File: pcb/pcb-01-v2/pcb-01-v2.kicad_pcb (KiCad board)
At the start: 2 copper layers, 0 parts

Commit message: Complete PCB-01 V2 KiCad scaffold
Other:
- copper layers 2 -> 4
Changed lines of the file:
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@@
 	)
 	(paper "A4")
+	(title_block
+		(title "PCB-01 V2 Controller")
+		(rev "V2")
+		(company "Stillair")
+		(comment 1 "Fresh 4-layer controller redesign")
+	)
 	(layers
 		(0 "F.Cu" signal)
+		(4 "In1.Cu" power)
+		(6 "In2.Cu" power)
 		(2 "B.Cu" signal)
 		(9 "F.Adhes" user "F.Adhesive")
@@
 	)
 	(setup
+		(stackup
+			(layer "F.SilkS"
+				(type "Top Silk Screen")
+			)
+			(layer "F.Paste"
+				(type "Top Solder Paste")
+			)
+			(layer "F.Mask"
+				(type "Top Solder Mask")
+				(thickness 0.01)
+			)
+			(layer "F.Cu"
+				(type "copper")
+				(thickness 0.07)
+			)
+			(layer "dielectric 1"
+				(type "prepreg")
+				(thickness 0.1)
+				(material "FR4")
+				(epsilon_r 4.5)
+				(loss_tangent 0.02)
+			)
+			(layer "In1.Cu"
+				(type "copper")
+				(thickness 0.035)
+			)
+			(layer "dielectric 2"
+				(type "core")
+				(thickness 1.17)
+				(material "FR4")
+				(epsilon_r 4.5)
+				(loss_tangent 0.02)
+			)
+			(layer "In2.Cu"
+				(type "copper")
+				(thickness 0.035)
+			)
+			(layer "dielectric 3"
+				(type "prepreg")
+				(thickness 0.1)
+				(material "FR4")
+				(epsilon_r 4.5)
+				(loss_tangent 0.02)
+			)
+			(layer "B.Cu"
+				(type "copper")
+				(thickness 0.07)
+			)
+			(layer "B.Mask"
+				(type "Bottom Solder Mask")
+				(thickness 0.01)
+			)
+			(layer "B.Paste"
+				(type "Bottom Solder Paste")
+			)
+			(layer "B.SilkS"
+				(type "Bottom Silk Screen")
+			)
+			(copper_finish "None")
+			(dielectric_constraints no)
+		)
 		(pad_to_mask_clearance 0.05)
 		(allow_soldermask_bridges_in_footprints no)
@@
 		(capping no)
 		(filling no)
+		(zone_defaults)
 		(pcbplotparams
 			(layerselection 0x00000000_00000000_55555555_5755f5ff)

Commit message: Build PCB-01 V2 ready-to-route project
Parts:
- added C1: 470uF 50V, Capacitor_THT:CP_Radial_D10.0mm_P5.00mm, F.Cu at (58.5, 64.5)
- added C10: 22uF 25V X7R 10%, Capacitor_SMD:C_1210_3225Metric, F.Cu at (91.0, 63.0)
- added C11: 1uF 50V X5R 10%, Capacitor_SMD:C_0603_1608Metric, F.Cu at (84.0, 57.5)
- added C12: 1uF 50V X5R 10%, Capacitor_SMD:C_0603_1608Metric, F.Cu at (80.3, 92.8)
- added C13: 47nF 100V X7R 10%, Capacitor_SMD:C_0805_2012Metric, F.Cu at (78.0, 88.0)
- added C14: 1uF 50V X5R 10%, Capacitor_SMD:C_0603_1608Metric, F.Cu at (88.4, 93.8)
- added C15: 1uF 50V X5R 10%, Capacitor_SMD:C_0603_1608Metric, F.Cu at (83.6, 88.3)
- added C16: 22uF 25V X7R 10%, Capacitor_SMD:C_1210_3225Metric, F.Cu at (69.8, 94.0)
- added C17: 22uF 25V X7R 10%, Capacitor_SMD:C_1210_3225Metric, F.Cu at (128.5, 61.5)
- added C18: 100nF 16V X7R 10%, Capacitor_SMD:C_0402_1005Metric, F.Cu at (123.0, 63.8)
- added C19: 1uF 25V X5R 10%, Capacitor_SMD:C_0402_1005Metric, F.Cu at (124.5, 63.8)
- added C2: 470uF 50V, Capacitor_THT:CP_Radial_D10.0mm_P5.00mm, F.Cu at (71.5, 64.5)
- added C20: 100nF 16V X7R 10% U12 bypass, Capacitor_SMD:C_0402_1005Metric, F.Cu at (120.5, 61.5)
- added C22: 100nF 16V X7R 10%, Capacitor_SMD:C_0402_1005Metric, F.Cu at (97.5, 99.0)
- added C23: 10uF 25V X5R 10%, Capacitor_SMD:C_0805_2012Metric, F.Cu at (104.0, 85.0)
- added C24: 100nF 16V X7R 10%, Capacitor_SMD:C_0402_1005Metric, F.Cu at (103.5, 100.0)
- added C25: 100nF 16V X7R 10%, Capacitor_SMD:C_0402_1005Metric, F.Cu at (105.3, 95.7)
- added C26: 10uF 63V X7R 10%, Capacitor_SMD:C_1210_3225Metric, F.Cu at (116.8, 104.0)
- added C27: 100nF 100V X7R 10%, Capacitor_SMD:C_0805_2012Metric, F.Cu at (105.7, 103.7)
- added C28: 10uF 25V X7R 10%, Capacitor_SMD:C_1210_3225Metric, F.Cu at (106.5, 108.6)
- added C29: 100nF 50V X7R 10%, Capacitor_SMD:C_0603_1608Metric, F.Cu at (125.8, 100.5)
- added C3: 10uF 50V X7R 10%, Capacitor_SMD:C_1210_3225Metric, F.Cu at (79.0, 100.5)
- added C30: 10nF 50V C0G 5%, Capacitor_SMD:C_0603_1608Metric, F.Cu at (111.0, 99.0)
- added C31: 10nF 50V X7R 10%, Capacitor_SMD:C_0402_1005Metric, F.Cu at (113.5, 100.8)
- added C33: 100nF 50V X7R 10%, Capacitor_SMD:C_0603_1608Metric, F.Cu at (126.3, 96.0)
- added C34: 100nF 50V C0G 1%, Capacitor_SMD:C_1206_3216Metric, F.Cu at (115.0, 94.0)
- added C35: 2.2uF 50V X5R 10%, Capacitor_SMD:C_0805_2012Metric, F.Cu at (116.0, 99.0)
- added C4: 10uF 50V X7R 10%, Capacitor_SMD:C_1210_3225Metric, F.Cu at (78.0, 78.5)
- added C41: 100nF 16V X7R 10%, Capacitor_SMD:C_0402_1005Metric, F.Cu at (133.3, 100.2)
- added C42: 100nF 16V X7R 10%, Capacitor_SMD:C_0402_1005Metric, F.Cu at (99.2, 81.5)
- added C43: 100nF 16V X7R 10%, Capacitor_SMD:C_0402_1005Metric, F.Cu at (106.2, 87.2)
- added C5: 100nF 50V X7R 10%, Capacitor_SMD:C_0603_1608Metric, F.Cu at (80.3, 96.0)
- added C7: 2.2uF 100V X7R 10%, Capacitor_SMD:C_1210_3225Metric, F.Cu at (76.5, 57.5)
- added C8: 100nF 100V X7R 10%, Capacitor_SMD:C_0805_2012Metric, F.Cu at (81.0, 61.0)
- added C9: 22uF 25V X7R 10%, Capacitor_SMD:C_1210_3225Metric, F.Cu at (91.5, 59.0)
- added D1: MMSZ5242B-7-F, Diode_SMD:D_SOD-123, F.Cu at (56.5, 84.5)
- added D2: SMCJ24A, Diode_SMD:D_SMC, F.Cu at (66.5, 87.0)
- added D3: BAT54W-G3-08, Diode_SMD:D_SOD-123, F.Cu at (89.5, 75.0)
- added D4: BAT54W-G3-08, Diode_SMD:D_SOD-123, F.Cu at (94.5, 75.0)
- added D5: BAT54W-G3-08, Diode_SMD:D_SOD-123, F.Cu at (99.5, 75.0)
- added D6: BAT54W-G3-08, Diode_SMD:D_SOD-123, F.Cu at (94.0, 78.5)
- added D7: BAT54W-G3-08, Diode_SMD:D_SOD-123, F.Cu at (90.0, 85.0)
- added D8: BAT54W-G3-08, Diode_SMD:D_SOD-123, F.Cu at (106.0, 82.0)
- added D9: BAT54SLT1G, Package_TO_SOT_SMD:SOT-23, F.Cu at (110.0, 96.0)
- added FID1: FIDUCIAL, Fiducial_1mm_Mask2mm, F.Cu at (125.0, 53.9)
- added FID2: FIDUCIAL, Fiducial_1mm_Mask2mm, F.Cu at (134.2, 62.0)
- added FID3: FIDUCIAL, Fiducial_1mm_Mask2mm, F.Cu at (63.0, 103.0)
- added H1: M3 NPTH, MountingHole_M3_3.2mm, F.Cu at (55.0, 55.0)
- added H2: M3 NPTH, MountingHole_M3_3.2mm, F.Cu at (133.0, 55.0)
- added H3: M3 NPTH, MountingHole_M3_3.2mm, F.Cu at (55.0, 109.0)
- added H4: M3 NPTH, MountingHole_M3_3.2mm, F.Cu at (133.0, 109.0)
- added J1: 43045-0200 POWER, Connector_Molex:Molex_Micro-Fit_3.0_43045-0200_2x01_P3.00mm_Horizontal, F.Cu at (56.5, 77.0)
- added J2: 43650-0300, Connector_Molex:Molex_Micro-Fit_3.0_43650-0300_1x03_P3.00mm_Horizontal, F.Cu at (88.5, 104.5)
- added J3: B3B-PH-K-S(LF)(SN), Connector_JST:JST_PH_B3B-PH-K_1x03_P2.00mm_Vertical, F.Cu at (118.0, 110.5)
- added J5: B5B-PH-K-S(LF)(SN), Connector_JST:JST_PH_B5B-PH-K_1x05_P2.00mm_Vertical, F.Cu at (91.0, 52.5)
- added L1: SWPA6045S470MT, Inductor_SMD:L_Sunlord_SWPA6045S, F.Cu at (76.0, 94.0)
- added NT1: PGND-AGND tie, NetTie:NetTie-2_SMD_Pad2.0mm, F.Cu at (84.0, 85.5)
- added Q1: DMP6023LE-13, Package_TO_SOT_SMD:SOT-223-3_TabPin2, F.Cu at (66.5, 77.0)
- added Q2: 2N7002K-7, Package_TO_SOT_SMD:SOT-23, F.Cu at (94.0, 91.0)
- added Q3: 2N7002K-7, Package_TO_SOT_SMD:SOT-23, F.Cu at (115.0, 88.5)
- added Q4: BC847BDW1T1G, Package_TO_SOT_SMD:SOT-363_SC-70-6, F.Cu at (109.5, 62.0)
- added R1: 10k, Resistor_SMD:R_0402_1005Metric, F.Cu at (60.5, 83.5)
- added R10: 100k 1%, Resistor_SMD:R_0402_1005Metric, F.Cu at (93.0, 88.5)
- added R11: 10k 1%, Resistor_SMD:R_0402_1005Metric, F.Cu at (103.0, 74.5)
- added R12: 10k 1%, Resistor_SMD:R_0402_1005Metric, F.Cu at (105.0, 74.5)
- added R13: 10k 1%, Resistor_SMD:R_0402_1005Metric, F.Cu at (103.0, 76.5)
- added R14: 100ohm 1%, Resistor_SMD:R_0402_1005Metric, F.Cu at (88.5, 81.0)
- added R15: 100ohm 1%, Resistor_SMD:R_0402_1005Metric, F.Cu at (90.7, 81.0)
- added R16: 0ohm I2C isolation link, Resistor_SMD:R_0402_1005Metric, F.Cu at (88.5, 83.0)
- added R17: 0ohm I2C isolation link, Resistor_SMD:R_0402_1005Metric, F.Cu at (90.7, 83.0)
- added R18: 10k 1%, Resistor_SMD:R_0402_1005Metric, F.Cu at (105.0, 76.5)
- added R19: 4.7k 1%, Resistor_SMD:R_0402_1005Metric, F.Cu at (113.0, 63.0)
- added R2: 100k, Resistor_SMD:R_0402_1005Metric, F.Cu at (60.5, 85.5)
- added R20: 4.7k 1%, Resistor_SMD:R_0402_1005Metric, F.Cu at (116.0, 63.0)
- added R24: 100ohm 1%, Resistor_SMD:R_0402_1005Metric, F.Cu at (93.0, 86.0)
- added R25: 100k 1%, Resistor_SMD:R_0402_1005Metric, F.Cu at (96.0, 86.0)
- added R26: 1k 1%, Resistor_SMD:R_0402_1005Metric, F.Cu at (91.0, 90.0)
- added R27: 100k 1%, Resistor_SMD:R_0402_1005Metric, F.Cu at (91.0, 92.0)
- added R28: 4.7k 1%, Resistor_SMD:R_0402_1005Metric, F.Cu at (89.0, 97.5)
- added R29: 10k 1%, Resistor_SMD:R_0402_1005Metric, F.Cu at (91.0, 96.0)
- added R3: 10k 1%, Resistor_SMD:R_0402_1005Metric, F.Cu at (91.0, 66.5)
- added R30: 10k 1%, Resistor_SMD:R_0402_1005Metric, F.Cu at (93.0, 96.0)
- added R31: 100k 1%, Resistor_SMD:R_0402_1005Metric, F.Cu at (95.0, 96.0)
- added R32: 10k 1%, Resistor_SMD:R_0402_1005Metric, F.Cu at (97.0, 93.0)
- added R33: 10k 1%, Resistor_SMD:R_0402_1005Metric, F.Cu at (99.0, 93.0)
- added R34: 10k 1%, Resistor_SMD:R_0402_1005Metric, F.Cu at (97.0, 95.0)
- added R35: 10k 1%, Resistor_SMD:R_0402_1005Metric, F.Cu at (99.0, 95.0)
- added R36: 100ohm 1%, Resistor_SMD:R_0402_1005Metric, F.Cu at (97.0, 97.0)
- added R37: 10k 1%, Resistor_SMD:R_0402_1005Metric, F.Cu at (99.0, 97.0)
- added R38: 100ohm 1%, Resistor_SMD:R_0402_1005Metric, F.Cu at (104.0, 91.0)
- added R39: 47ohm 1W 1%, Resistor_SMD:R_2512_6332Metric, F.Cu at (84.5, 69.5)
- added R4: 4.7k 1%, Resistor_SMD:R_0402_1005Metric, F.Cu at (85.0, 77.0)
- added R40: 910k 0.1%, Resistor_SMD:R_0402_1005Metric, F.Cu at (108.0, 87.0)
- added R41: 100k 0.1%, Resistor_SMD:R_0402_1005Metric, F.Cu at (110.0, 87.0)
- added R42: 10k 1%, Resistor_SMD:R_0402_1005Metric, F.Cu at (108.0, 89.0)
- added R43: 10k 1%, Resistor_SMD:R_0402_1005Metric, F.Cu at (110.0, 89.0)
- added R44: 10k 1%, Resistor_SMD:R_0402_1005Metric, F.Cu at (108.0, 91.0)
- added R45: 100ohm 1%, Resistor_SMD:R_0402_1005Metric, F.Cu at (110.0, 91.0)
- added R46: 10k 1%, Resistor_SMD:R_0402_1005Metric, F.Cu at (108.0, 93.0)
- added R47: 10k 1%, Resistor_SMD:R_0402_1005Metric, F.Cu at (110.0, 93.0)
- added R48: 562k 1%, Resistor_SMD:R_0402_1005Metric, F.Cu at (121.0, 103.0)
- added R49: 10k 1%, Resistor_SMD:R_0402_1005Metric, F.Cu at (123.0, 103.0)
- added R5: 4.7k 1%, Resistor_SMD:R_0402_1005Metric, F.Cu at (87.2, 77.0)
- added R50: 10k 1%, Resistor_SMD:R_0402_1005Metric, F.Cu at (125.0, 103.0)
- added R51: 47.0k 0.1%, Resistor_SMD:R_0402_1005Metric, F.Cu at (121.0, 105.0)
- added R52: 10.0k 0.1%, Resistor_SMD:R_0402_1005Metric, F.Cu at (123.0, 105.0)
- added R53: 35.7k 1%, Resistor_SMD:R_0402_1005Metric, F.Cu at (125.0, 105.0)
- added R54: 90.9k 0.1%, Resistor_SMD:R_0402_1005Metric, F.Cu at (127.0, 107.0)
- added R55: 10k 1%, Resistor_SMD:R_0402_1005Metric, F.Cu at (108.5, 57.0)
- added R56: 10k 1%, Resistor_SMD:R_0402_1005Metric, F.Cu at (110.5, 57.0)
- added R57: 470ohm UART RX series, Resistor_SMD:R_0402_1005Metric, F.Cu at (109.5, 64.5)
- added R6: 4.7k 1%, Resistor_SMD:R_0402_1005Metric, F.Cu at (85.0, 79.0)
- added R7: 4.7k 1%, Resistor_SMD:R_0402_1005Metric, F.Cu at (87.2, 79.0)
- added R8: 10k 1%, Resistor_SMD:R_0402_1005Metric, F.Cu at (89.0, 87.0)
- added R9: 10k 1%, Resistor_SMD:R_0402_1005Metric, F.Cu at (91.0, 87.0)
- added RV1: 3224W-1-204E, Potentiometer_SMD:Potentiometer_Bourns_3224W_Vertical, F.Cu at (130.0, 88.5)
- added SW1: PTS645SK43SMTR92LFS, Button_Switch_SMD:SW_SPST_PTS645Sx43SMTR92, F.Cu at (103.0, 61.0)
- added SW2: PTS645SK43SMTR92LFS, Button_Switch_SMD:SW_SPST_PTS645Sx43SMTR92, F.Cu at (103.0, 69.0)
- added SW3: PTS645SK43SMTR92LFS, Button_Switch_SMD:SW_SPST_PTS645Sx43SMTR92, F.Cu at (99.5, 110.0)
- added TP1: RAW24, pcb01-v2-parts:TestHole_2.4mm_PTH1.0mm, F.Cu at (52.0, 62.0)
- added TP10: TP10, pcb01-v2-parts:TestHole_2.4mm_PTH1.0mm, F.Cu at (61.5, 53.0)
- added TP11: TP11, pcb01-v2-parts:TestHole_2.4mm_PTH1.0mm, F.Cu at (65.0, 53.0)
- added TP12: TP12, pcb01-v2-parts:TestHole_2.4mm_PTH1.0mm, F.Cu at (69.0, 53.0)
- added TP13: TP13, pcb01-v2-parts:TestHole_2.4mm_PTH1.0mm, F.Cu at (73.0, 53.0)
- added TP14: TP14, pcb01-v2-parts:TestHole_2.4mm_PTH1.0mm, F.Cu at (77.0, 53.0)
- added TP15: TP15, pcb01-v2-parts:TestHole_2.4mm_PTH1.0mm, F.Cu at (136.0, 94.0)
- added TP16: TP16, pcb01-v2-parts:TestHole_2.4mm_PTH1.0mm, F.Cu at (81.0, 53.0)
- added TP17: TP17, pcb01-v2-parts:TestHole_2.4mm_PTH1.0mm, F.Cu at (69.5, 106.5)
- added TP18: TP18, pcb01-v2-parts:TestHole_2.4mm_PTH1.0mm, F.Cu at (70.0, 111.5)
- added TP19: TP19, pcb01-v2-parts:TestHole_2.4mm_PTH1.0mm, F.Cu at (114.0, 53.0)
- added TP2: VM24, pcb01-v2-parts:TestHole_2.4mm_PTH1.0mm, F.Cu at (52.0, 66.0)
- added TP20: TP20, pcb01-v2-parts:TestHole_2.4mm_PTH1.0mm, F.Cu at (118.0, 53.0)
- added TP21: TP21, pcb01-v2-parts:TestHole_2.4mm_PTH1.0mm, F.Cu at (136.0, 98.0)
- added TP22: TP22, pcb01-v2-parts:TestHole_2.4mm_PTH1.0mm, F.Cu at (136.0, 102.0)
- added TP23: TP23, pcb01-v2-parts:TestHole_2.4mm_PTH1.0mm, F.Cu at (127.0, 111.5)
- added TP24: TP24, pcb01-v2-parts:TestHole_2.4mm_PTH1.0mm, F.Cu at (83.0, 73.5)
- added TP25: TP25, pcb01-v2-parts:TestHole_2.4mm_PTH1.0mm, F.Cu at (79.0, 73.5)
- added TP26: TP26, pcb01-v2-parts:TestHole_2.4mm_PTH1.0mm, F.Cu at (75.0, 73.5)
- added TP27: TP27, pcb01-v2-parts:TestHole_2.4mm_PTH1.0mm, F.Cu at (52.0, 97.0)
- added TP28: TP28, pcb01-v2-parts:TestHole_2.4mm_PTH1.0mm, F.Cu at (58.5, 96.0)
- added TP29: TP29, pcb01-v2-parts:TestHole_2.4mm_PTH1.0mm, F.Cu at (58.5, 92.0)
- added TP3: PGND, pcb01-v2-parts:TestHole_2.4mm_PTH1.0mm, F.Cu at (52.0, 85.0)
- added TP30: TP30, pcb01-v2-parts:TestHole_2.4mm_PTH1.0mm, F.Cu at (106.0, 53.0)
- added TP31: TP31, pcb01-v2-parts:TestHole_2.4mm_PTH1.0mm, F.Cu at (110.0, 53.0)
- added TP4: AGND, pcb01-v2-parts:TestHole_2.4mm_PTH1.0mm, F.Cu at (52.0, 89.0)
- added TP5: TP5, pcb01-v2-parts:TestHole_2.4mm_PTH1.0mm, F.Cu at (52.0, 93.0)
- added TP6: TP6, pcb01-v2-parts:TestHole_2.4mm_PTH1.0mm, F.Cu at (136.0, 88.0)
- added TP7: TP7, pcb01-v2-parts:TestHole_2.4mm_PTH1.0mm, F.Cu at (62.0, 111.5)
- added TP8: TP8, pcb01-v2-parts:TestHole_2.4mm_PTH1.0mm, F.Cu at (66.0, 111.5)
- added TP9: TP9, pcb01-v2-parts:TestHole_2.4mm_PTH1.0mm, F.Cu at (85.0, 53.0)
- added U1: MCF8316DVRGFR, MCF8316D_RGF0040E, F.Cu at (84.0, 94.0)
- added U10: SN74LVC1G17DCKR, Package_TO_SOT_SMD:SOT-353_SC-70-5, F.Cu at (94.0, 102.0)
- added U11: SN74LVC1G17DCKR, Package_TO_SOT_SMD:SOT-353_SC-70-5, F.Cu at (101.0, 102.0)
- added U12: TMP1075DGKR, pcb01-v2-parts:VSSOP-8_3x3mm_P0.65mm_Clearance0.20, F.Cu at (116.0, 58.5)
- added U2: ESP32-C6-WROOM-1-N8, ESP32-C6-WROOM-1, F.Cu at (122.3, 75.0)
- added U3: TPSM365R6V3RDNR, TPSM365R6_RDN0011A, F.Cu at (85.5, 62.0)
- added U4: TPS7A1601ADGNR, Package_SO:MSOP-8-1EP_3x3mm_P0.65mm_EP1.68x1.88mm, F.Cu at (111.0, 104.0)
- added U5: SN74LVC1G74DCTR, pcb01-parts:TI_SM8_DCT0008A, F.Cu at (96.0, 82.0)
- added U6: SN74LVC1G74DCTR, pcb01-parts:TI_SM8_DCT0008A, F.Cu at (102.0, 88.0)
- added U7: TPS3435CAKAGDDFR, pcb01-v2-parts:SOT-23-8_P0.65mm_Clearance0.20, F.Cu at (102.0, 96.0)
- added U8: LM2907M-14/NOPB, Package_SO:SOIC-14_3.9x8.7mm_P1.27mm, F.Cu at (121.0, 96.0)
- added U9: TLV1701AIDBVR, Package_TO_SOT_SMD:SOT-23-5, F.Cu at (130.0, 101.5)
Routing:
- added copper zone on In2.Cu, net 3V3
- added copper zone on B.Cu, net AGND
- added copper zone on In1.Cu, net AGND
- added copper zone on In2.Cu, net AGND
- added copper zone on In1.Cu, net PGND
- added copper zone on In2.Cu, net VM24
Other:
- board outline added: 88 x 64 mm
- rule pad_to_mask_clearance: 0.05 -> 0
- board text added: "+"
- board text added: "1"
- board text added: "1:+24 2:PGND"
- board text added: "1:3V3 2:HALL 3:GND"
- board text added: "3:U 2:V 1:W"
- board text added: "4:RTS 5:DTR"
- board text added: "ANTENNA"
- board text added: "BOOT"
- board text added: "CCW INC"
- board text added: "CLEAR"
- board text added: "CW DEC"
- board text added: "DIFF PROBE ONLY"
- board text added: "J1 POWER"
- board text added: "J2 MOTOR"
- board text added: "J3 HALL"
- board text added: "J5/UART 1:GND 2:TX 3:RX"
- board text added: "K"
- board text added: "OVERSPEED CAL"
- board text added: "PCB-01 V2"
- board text added: "PCB-01 V2 TEST POINT MAP"
- board text added: "RESET"
- board text added: "TP1"
- board text added: "TP1 RAW24"
- board text added: "TP10"
- board text added: "TP10 U5_CLR_OR"
- board text added: "TP11"
- board text added: "TP11 U5_Q"
- board text added: "TP12"
- board text added: "TP12 DRVOFF"
- board text added: "TP13"
- board text added: "TP13 WD_HEARTBEAT"
- board text added: "TP14"
- board text added: "TP14 WDO"
- board text added: "TP15"
- board text added: "TP15 OVERSPEED_N"
- board text added: "TP16"
- board text added: "TP16 MCF_EXT_WD"
- board text added: "TP17"
- board text added: "TP17 NFAULT"
- board text added: "TP18"
- board text added: "TP18 SDA"
- board text added: "TP19"
- board text added: "TP19 SCL"
- board text added: "TP2"
- board text added: "TP2 VM24"
- board text added: "TP20"
- board text added: "TP20 FG"
- board text added: "TP21"
- board text added: "TP21 HALL_TACH"
- board text added: "TP22"
- board text added: "TP22 VTACH"
- board text added: "TP23"
- board text added: "TP23 VREF"
- board text added: "TP24"
- board text added: "TP24 SOX"
- board text added: "TP25"
- board text added: "TP25 SPEED"
- board text added: "TP26"
- board text added: "TP26 ALARM"
- board text added: "TP27"
- board text added: "TP27 WD_MR"
- board text added: "TP28"
- board text added: "TP28 U7_WDI"
- board text added: "TP29"
- board text added: "TP29 WD_EN"
- board text added: "TP3"
- board text added: "TP3 PGND"
- board text added: "TP30"
- board text added: "TP30 TEMP_SDA"
- board text added: "TP31"
- board text added: "TP31 TEMP_SCL"
- board text added: "TP4"
- board text added: "TP4 AGND"
- board text added: "TP5"
- board text added: "TP5 3V3"
- board text added: "TP6"
- board text added: "TP6 +12V_TACH"
- board text added: "TP7"
- board text added: "TP7 MCF_AVDD"
- board text added: "TP8"
- board text added: "TP8 MCF_DVDD"
- board text added: "TP9"
- board text added: "TP9 PGOOD"

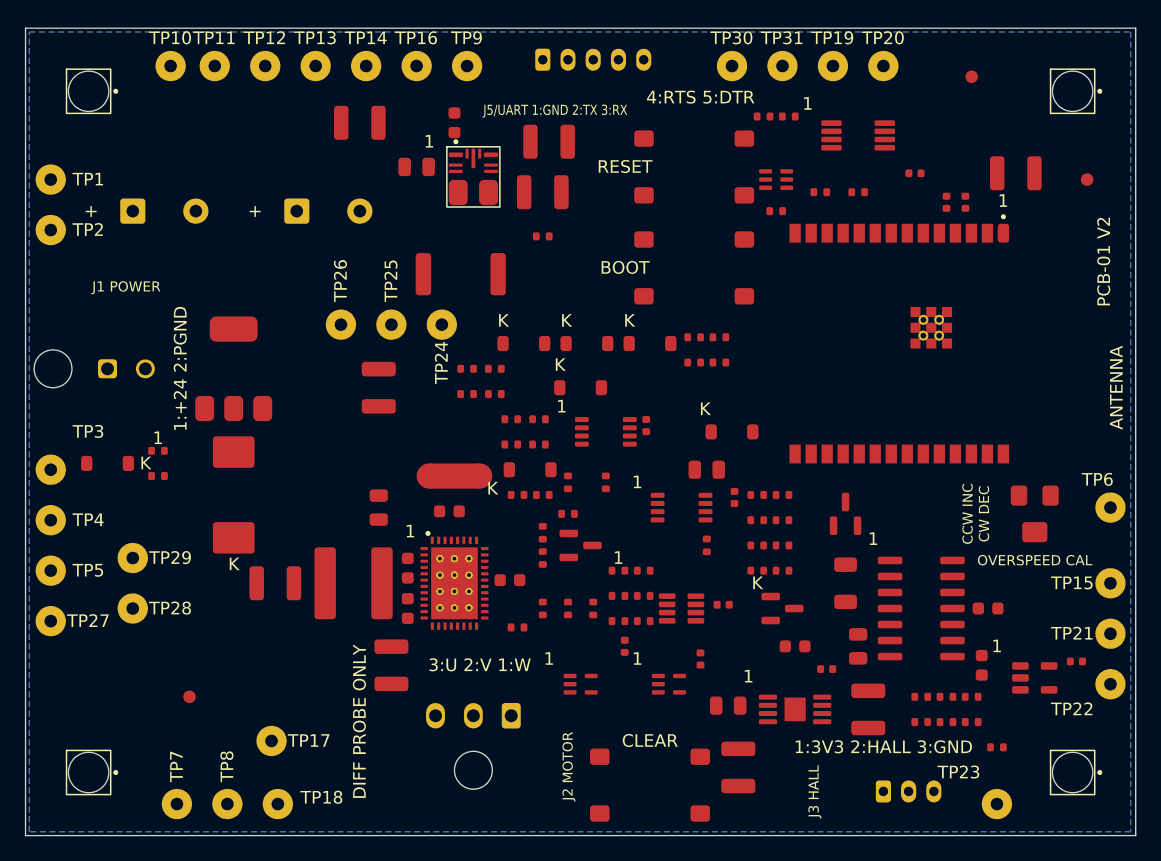
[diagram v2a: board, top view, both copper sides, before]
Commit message: Redesign PCB-01 V2 for native USB-C
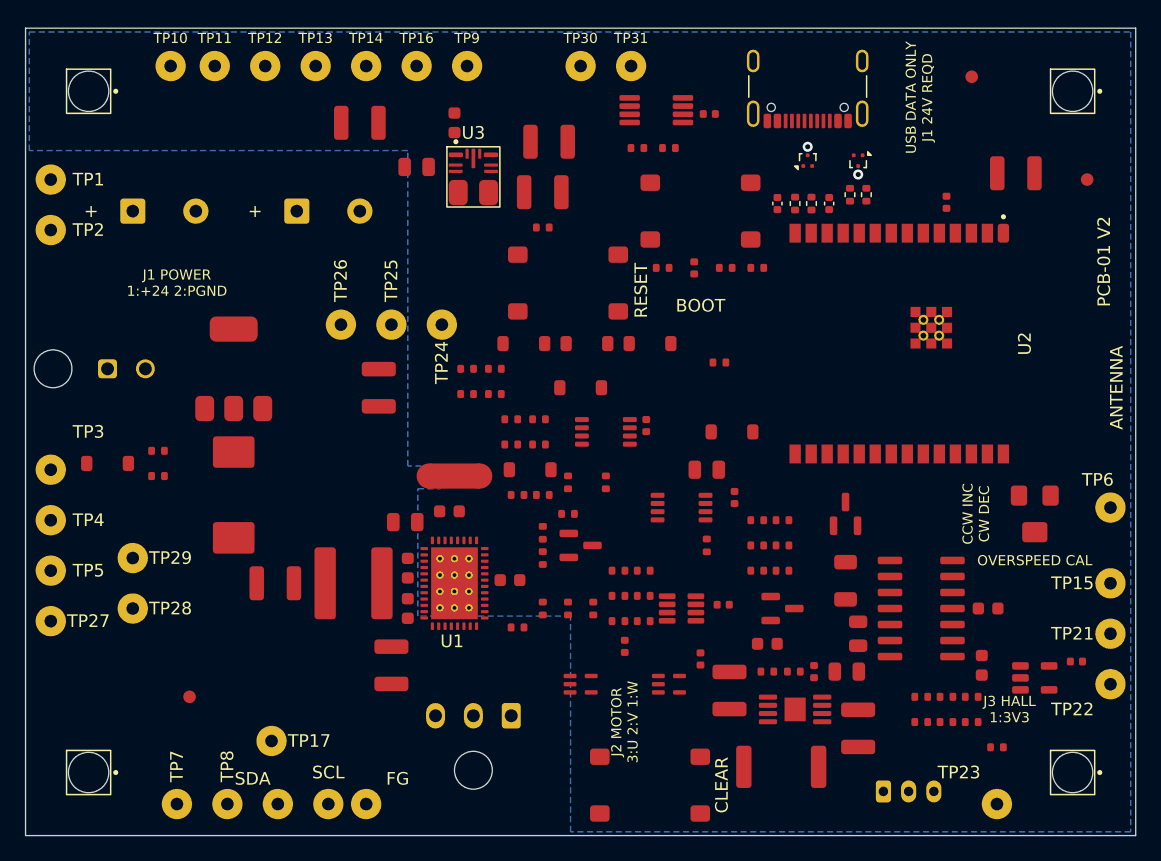
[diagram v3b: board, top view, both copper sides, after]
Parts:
- removed J5: B5B-PH-K-S(LF)(SN), Connector_JST:JST_PH_B5B-PH-K_1x05_P2.00mm_Vertical
- removed Q4: BC847BDW1T1G, Package_TO_SOT_SMD:SOT-363_SC-70-6
- removed R55, R56: 10k 1%, Resistor_SMD:R_0402_1005Metric
- removed R57: 470ohm UART RX series, Resistor_SMD:R_0402_1005Metric
- added C44: DNP USB tuning, Capacitor_SMD:C_0402_1005Metric, F.Cu at (109.6, 63.9)
- added C45: DNP USB tuning, Capacitor_SMD:C_0402_1005Metric, F.Cu at (113.7, 63.9)
- added J4: USB4105-GF-A, Connector_USB:USB_C_Receptacle_GCT_USB4105-xx-A_16P_TopMnt_Horizontal, F.Cu at (112.0, 53.7)
- added R58: 22R, Resistor_SMD:R_0402_1005Metric, F.Cu at (111.0, 63.9)
- added R59: 22R, Resistor_SMD:R_0402_1005Metric, F.Cu at (112.3, 63.9)
- added R60: 5.1k, Resistor_SMD:R_0402_1005Metric, F.Cu at (116.7, 63.2)
- added R61: 5.1k, Resistor_SMD:R_0402_1005Metric, F.Cu at (115.3, 63.2)
- added U13: TPD2EUSB30DRTR, Package_TO_SOT_SMD:Texas_DRT-3, F.Cu at (112.0, 60.5)
- added U14: TPD2EUSB30DRTR, Package_TO_SOT_SMD:Texas_DRT-3, F.Cu at (116.0, 60.5)
- U1: footprint MCF8316D_RGF0040E -> pcb01-parts:MCF8316D_RGF0040E
- U2: footprint ESP32-C6-WROOM-1 -> pcb01-v2-parts:ESP32-C6-WROOM-1
- U3: footprint TPSM365R6_RDN0011A -> pcb01-parts:TPSM365R6_RDN0011A
- moved TP20 71.4 mm to (77.0, 111.5)
- moved TP19 70.9 mm to (74.0, 111.5)
- moved R39 46.6 mm to (109.9, 108.5), turned to 0 degrees
- moved C19 22.1 mm to (103.0, 69.0)
- moved C20 17.0 mm to (104.2, 56.8)
- moved U12 16.1 mm to (100.0, 56.5)
- moved R20 15.4 mm to (101.0, 59.5)
- moved R19 14.9 mm to (98.5, 59.5)
- moved R41 14.0 mm to (110.9, 101.0)
- moved R40 14.0 mm to (108.8, 101.0)
- moved SW1 13.6 mm to (93.0, 70.2)
- moved TP30 12.0 mm to (94.0, 53.0)
- moved TP31 12.0 mm to (98.0, 53.0)
- moved C27 9.78 mm to (115.1, 101.0), turned to 0 degrees
- moved R13 9.01 mm to (108.0, 69.0)
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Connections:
- U1 pad 22: (no net) -> unconnected-(U1-NC-Pad22)
- U1 pad 23: (no net) -> unconnected-(U1-NC-Pad23)
- U1 pad 24: (no net) -> unconnected-(U1-NC-Pad24)
- U1 pad 25: (no net) -> unconnected-(U1-NC-Pad25)
- U1 pad 33: (no net) -> unconnected-(U1-EXT_CLK-Pad33)
- U1 pad 36: (no net) -> unconnected-(U1-DACOUT1-Pad36)
- U1 pad 37: (no net) -> unconnected-(U1-DACOUT2-Pad37)
- U2 pad 13: (no net) -> /SCH-04 Supervisor + Service/USB_D_MCU_N
- U2 pad 14: (no net) -> /SCH-04 Supervisor + Service/USB_D_MCU_P
- U2 pad 22: (no net) -> unconnected-(U2-NC-Pad22)
- U2 pad 24: UART_RX -> unconnected-(U2-RXD0-Pad24)
- U2 pad 25: UART_TX -> unconnected-(U2-TXD0-Pad25)
- U2 pad 4: (no net) -> unconnected-(U2-IO4-Pad4)
- U2 pad 5: (no net) -> unconnected-(U2-IO5-Pad5)
- U3 pad 5: (no net) -> unconnected-(U3-SW-Pad5)
- U3 pad 6: (no net) -> unconnected-(U3-SW-Pad6)
- U3 pad 7: (no net) -> unconnected-(U3-BOOT-Pad7)
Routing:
- net AGND: vias 0 -> 2
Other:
- board text added: "FG"
- board text added: "J1 24V REQD"
- board text added: "J1 POWER 1:+24 2:PGND"
- board text added: "J2 MOTOR 3:U 2:V 1:W"
- board text added: "J3 HALL 1:3V3"
- board text added: "SCL"
- board text added: "SDA"
- board text added: "USB DATA ONLY"
- board text removed: "1"
- board text removed: "1:+24 2:PGND"
- board text removed: "3:U 2:V 1:W"
- board text removed: "4:RTS 5:DTR"
- board text removed: "DIFF PROBE ONLY"
- board text removed: "J1 POWER"
- board text removed: "J2 MOTOR"
- board text removed: "J3 HALL"
- board text removed: "J5/UART 1:GND 2:TX 3:RX"
- board text removed: "K"
- board text removed: "TP18"
- board text removed: "TP18 SDA"
- board text removed: "TP19"
- board text removed: "TP19 SCL"
- board text removed: "TP20"
- board text removed: "TP20 FG"

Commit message: Open U1 routing clearance
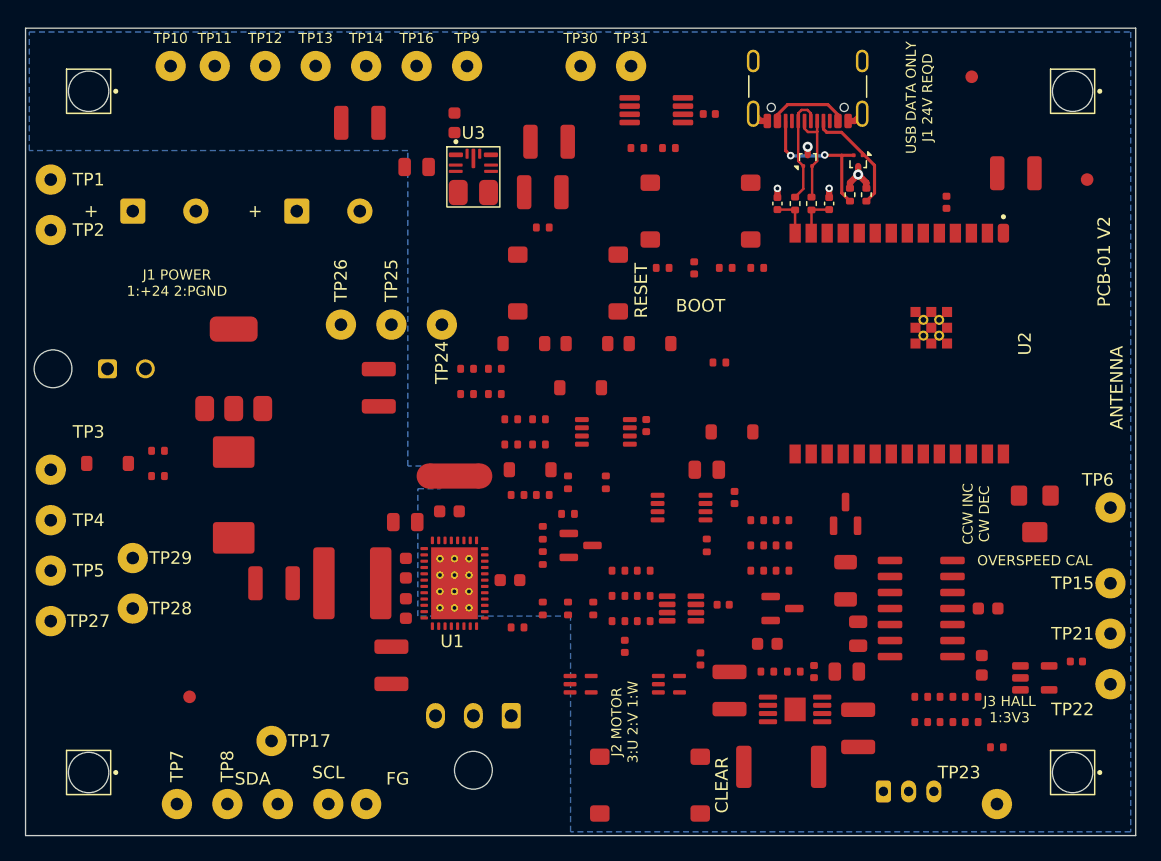
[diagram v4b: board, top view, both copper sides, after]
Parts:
- moved C12 0.15 mm to (80.2, 92.8)
- moved C5 0.15 mm to (80.2, 96.0)
- moved C16 0.10 mm to (69.7, 94.0)
- moved L1 0.10 mm to (75.9, 94.0)
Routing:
- net /SCH-04 Supervisor + Service/USB_CC2: track 0.00 -> 11.9 mm, vias 0 -> 2
- net /SCH-04 Supervisor + Service/USB_CC1: track 0.00 -> 9.13 mm
- net /SCH-04 Supervisor + Service/USB_DP: track 0.00 -> 8.91 mm
- net AGND: track 0.00 -> 8.22 mm, vias 2 -> 4
- net /SCH-04 Supervisor + Service/USB_DN: track 0.00 -> 7.95 mm
- net /SCH-04 Supervisor + Service/USB_VBUS: track 0.00 -> 6.45 mm
- net /SCH-04 Supervisor + Service/USB_D_MCU_N: track 0.00 -> 3.26 mm
- net /SCH-04 Supervisor + Service/USB_D_MCU_P: track 0.00 -> 3.25 mm

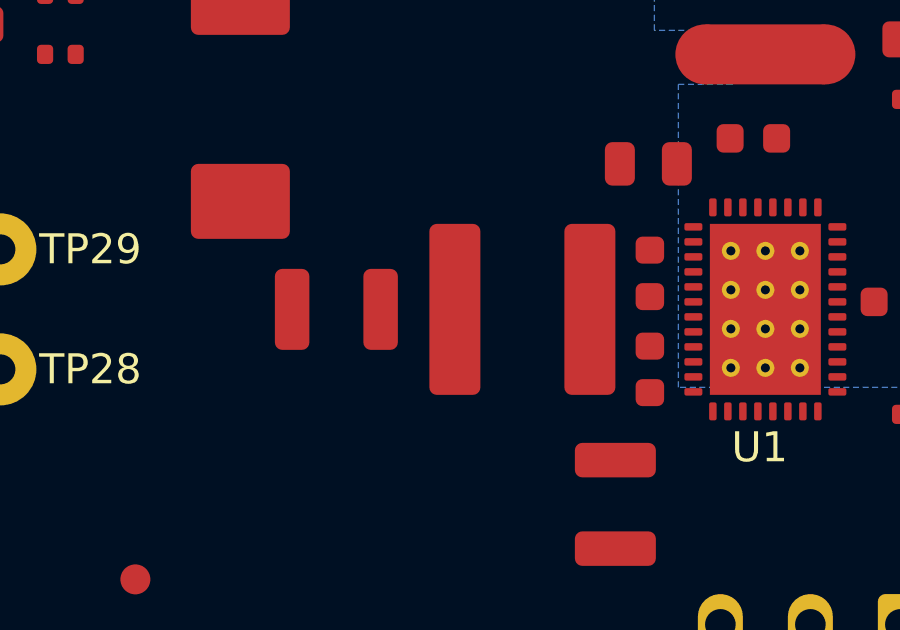
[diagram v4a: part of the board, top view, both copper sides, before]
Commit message: Widen U1 routing channels
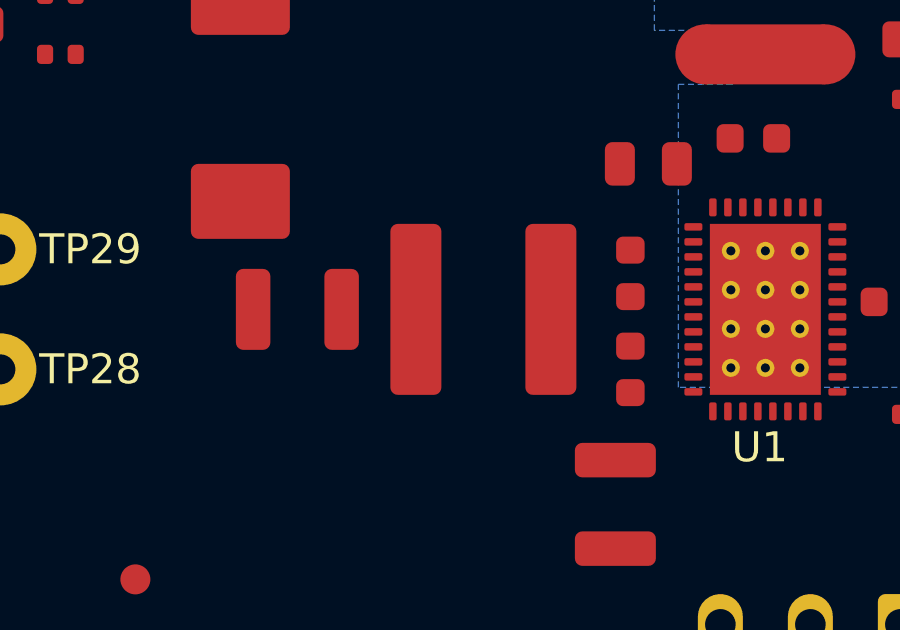
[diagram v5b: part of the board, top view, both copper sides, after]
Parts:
- moved L1 1.30 mm to (74.6, 94.0)
- moved C16 1.30 mm to (68.4, 94.0)
- moved C12 0.65 mm to (79.5, 92.8)
- moved C5 0.65 mm to (79.5, 96.0)
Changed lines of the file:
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@@
 	(footprint "Capacitor_SMD:C_0603_1608Metric"
 		(layer "F.Cu")
-		(at 80.15 92.8 -90)
+		(at 79.5 92.8 -90)
 		(descr "Capacitor SMD 0603 (1608 Metric), square (rectangular) end terminal, IPC-7351 nominal, (Body size source: IPC-SM-782 page 76, https://www.pcb-3d.com/wordpress/wp-content/uploads/ipc-sm-782a_amendment_1_and_2.pdf)")
 		(tags "capacitor")
@@
 	(footprint "Inductor_SMD:L_Sunlord_SWPA6045S"
 		(layer "F.Cu")
-		(at 75.9 94 180)
+		(at 74.6 94 180)
 		(descr "Inductor, Sunlord, SWPA6045S, 6.0x6.0x4.5mm, (https://www.sunlordinc.com/UploadFiles/PDF_Cat/20120704094224784.pdf)")
 		(tags "swpa")
@@
 	(footprint "Capacitor_SMD:C_1210_3225Metric"
 		(layer "F.Cu")
-		(at 69.7 94 180)
+		(at 68.4 94 180)
 		(descr "Capacitor SMD 1210 (3225 Metric), square (rectangular) end terminal, IPC-7351 nominal, (Body size source: IPC-SM-782 page 76, https://www.pcb-3d.com/wordpress/wp-content/uploads/ipc-sm-782a_amendment_1_and_2.pdf)")
 		(tags "capacitor")
@@
 	(footprint "Capacitor_SMD:C_0603_1608Metric"
 		(layer "F.Cu")
-		(at 80.15 96 -90)
+		(at 79.5 96 -90)
 		(descr "Capacitor SMD 0603 (1608 Metric), square (rectangular) end terminal, IPC-7351 nominal, (Body size source: IPC-SM-782 page 76, https://www.pcb-3d.com/wordpress/wp-content/uploads/ipc-sm-782a_amendment_1_and_2.pdf)")
 		(tags "capacitor")

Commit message: Open U1 power fanout corridor
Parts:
- moved C12 2.00 mm to (77.5, 92.8)
- moved C16 2.00 mm to (66.4, 94.0)
- moved C3 2.00 mm to (77.0, 100.5)
- moved C5 2.00 mm to (77.5, 96.0)
- moved L1 2.00 mm to (72.6, 94.0)
- moved D2 1.00 mm to (65.5, 87.0)
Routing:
- net MCF_AVDD: track 0.00 -> 48.2 mm, vias 0 -> 1
- net MCF_DVDD: track 0.00 -> 35.8 mm, vias 0 -> 1
- net MCF_CPH: track 0.00 -> 6.54 mm, vias 0 -> 2
- net MCF_CPL: track 0.00 -> 6.04 mm, vias 0 -> 2
